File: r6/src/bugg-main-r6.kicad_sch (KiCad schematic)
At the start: 46 parts, among them T14 , T15 , T16 , T3 , T39 , T40 , U1 74LVC1G07DCK, U34 74LVC1G157GV

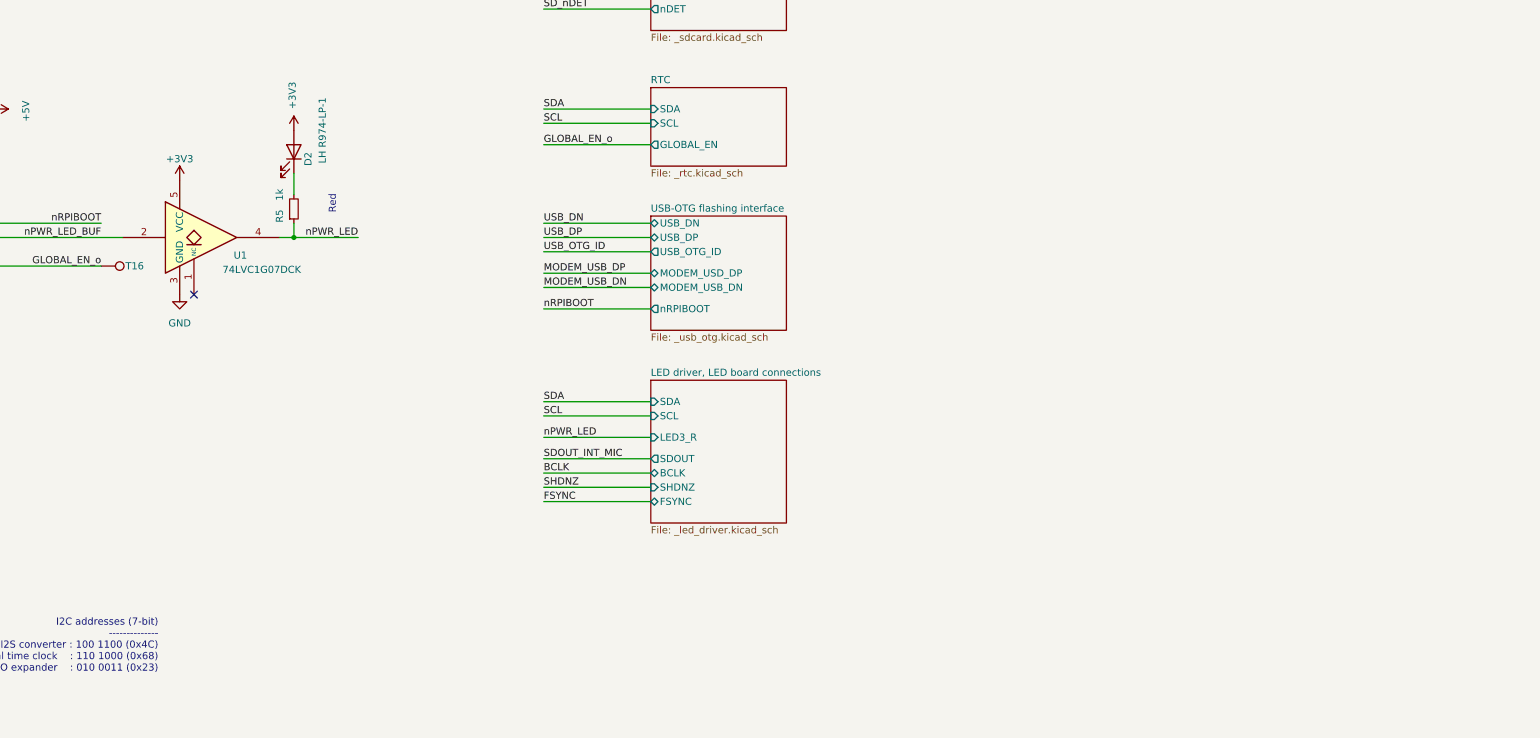
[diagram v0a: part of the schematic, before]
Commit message: r6: experimental revision of the r5 main board (unbuilt)
Filtered plug-in mic bias (R104 100R, Q25 supplied ahead of it),
4.7 nF ADC input filter, RV-3032 RTC on a new 3.3 V always-on rail,
Schmitt wake buffer, ADS1115 four-rail voltage monitoring, and a latched
modem SAFE_PWR_REMOVE/VGPIO shutdown confirmation (r5 erratum 5).

Outline, stack, all 37 fixed interfaces, USB and mic-input copper and
all r5 test points are unchanged. Designed and routed with AI coding
agents, reviewed by the author. No board has been built or measured.
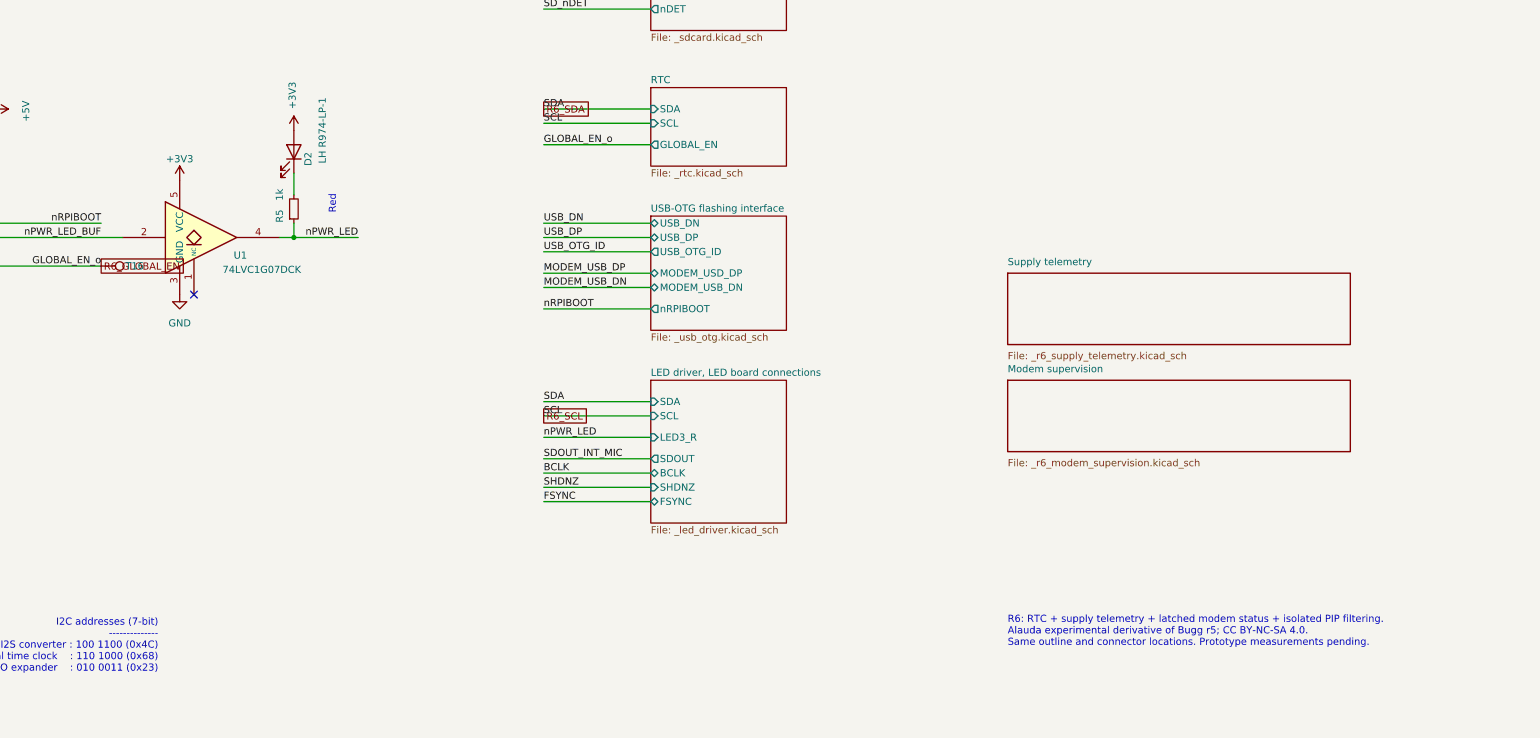
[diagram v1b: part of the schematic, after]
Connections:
- net GLOBAL_EN_o renamed R6_GLOBAL_EN
- net SCL renamed R6_SCL
- net SDA renamed R6_SDA
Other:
- added sheet Modem supervision (_r6_modem_supervision.kicad_sch)
- added sheet Supply telemetry (_r6_supply_telemetry.kicad_sch)
- note added: "R6: RTC + supply telemetry + latched modem status + isolated PIP filtering. Alauda experimental derivative of Bugg r5; CC BY-NC-SA 4.0. Same outline and connector locations. Prototype measurements pending."
